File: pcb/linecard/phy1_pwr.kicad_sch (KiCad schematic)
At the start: 169 parts, among them U35 VSC8512

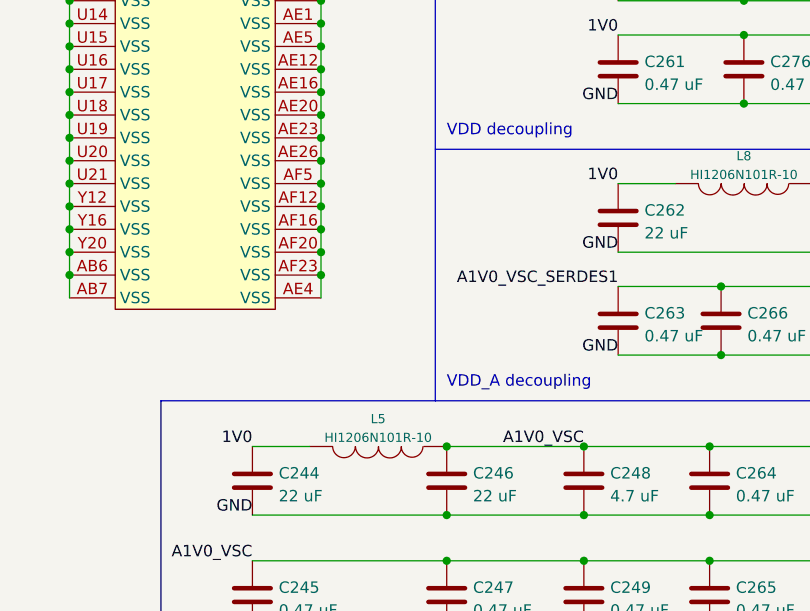
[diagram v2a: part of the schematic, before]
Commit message: Finished routing of left PHY
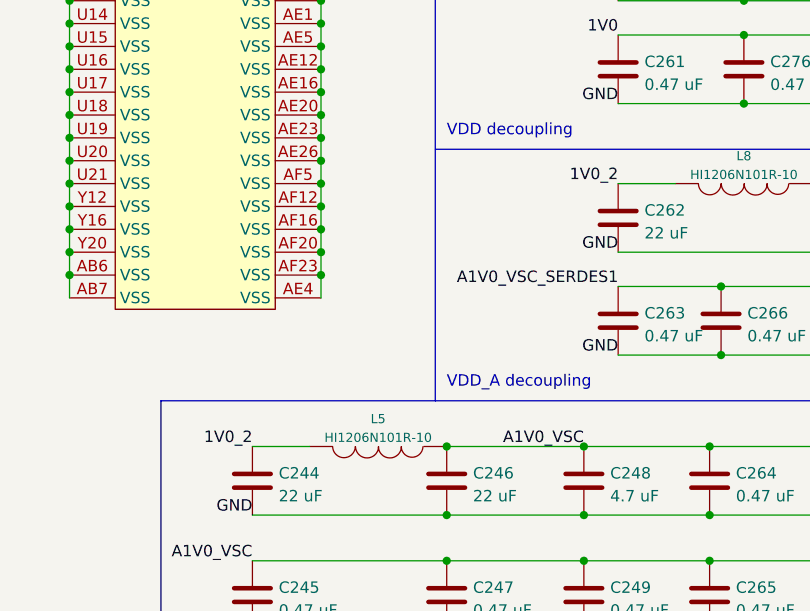
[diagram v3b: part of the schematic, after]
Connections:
- net 1V0: no longer C244.1, C262.1, L5.2, L8.2
- net 1V0_2: now also C244.1, C262.1, L5.2, L8.2
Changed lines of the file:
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@@
 	(title_block
 		(title "LATENTRED Line Card")
-		(date "2024-12-13")
+		(date "2024-12-14")
 		(rev "0.1")
 		(company "Antikernel Labs")
@@
 		)
 	)
-	(label "1V0"
+	(label "1V0_2"
 		(at 232.41 198.12 180)
 		(fields_autoplaced yes)
@@
 		)
 	)
-	(label "1V0"
+	(label "1V0_2"
 		(at 191.77 227.33 180)
 		(fields_autoplaced yes)

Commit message: Continued routing right PHY
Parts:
- C278: footprint azonenberg_pcb:EIA_1206_CAP_NOSILK -> azonenberg_pcb:EIA_1210_CAP_NOSILK
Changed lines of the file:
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@@
 	(title_block
 		(title "LATENTRED Line Card")
-		(date "2024-12-18")
+		(date "2024-12-19")
 		(rev "0.1")
 		(company "Antikernel Labs")
@@
 			)
 		)
-		(property "Footprint" "azonenberg_pcb:EIA_1206_CAP_NOSILK"
+		(property "Footprint" "azonenberg_pcb:EIA_1210_CAP_NOSILK"
 			(at 257.5052 205.74 0)
 			(effects
